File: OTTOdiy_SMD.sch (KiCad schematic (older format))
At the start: 20 parts, among them J201 RASPBERRY PI 3 A+

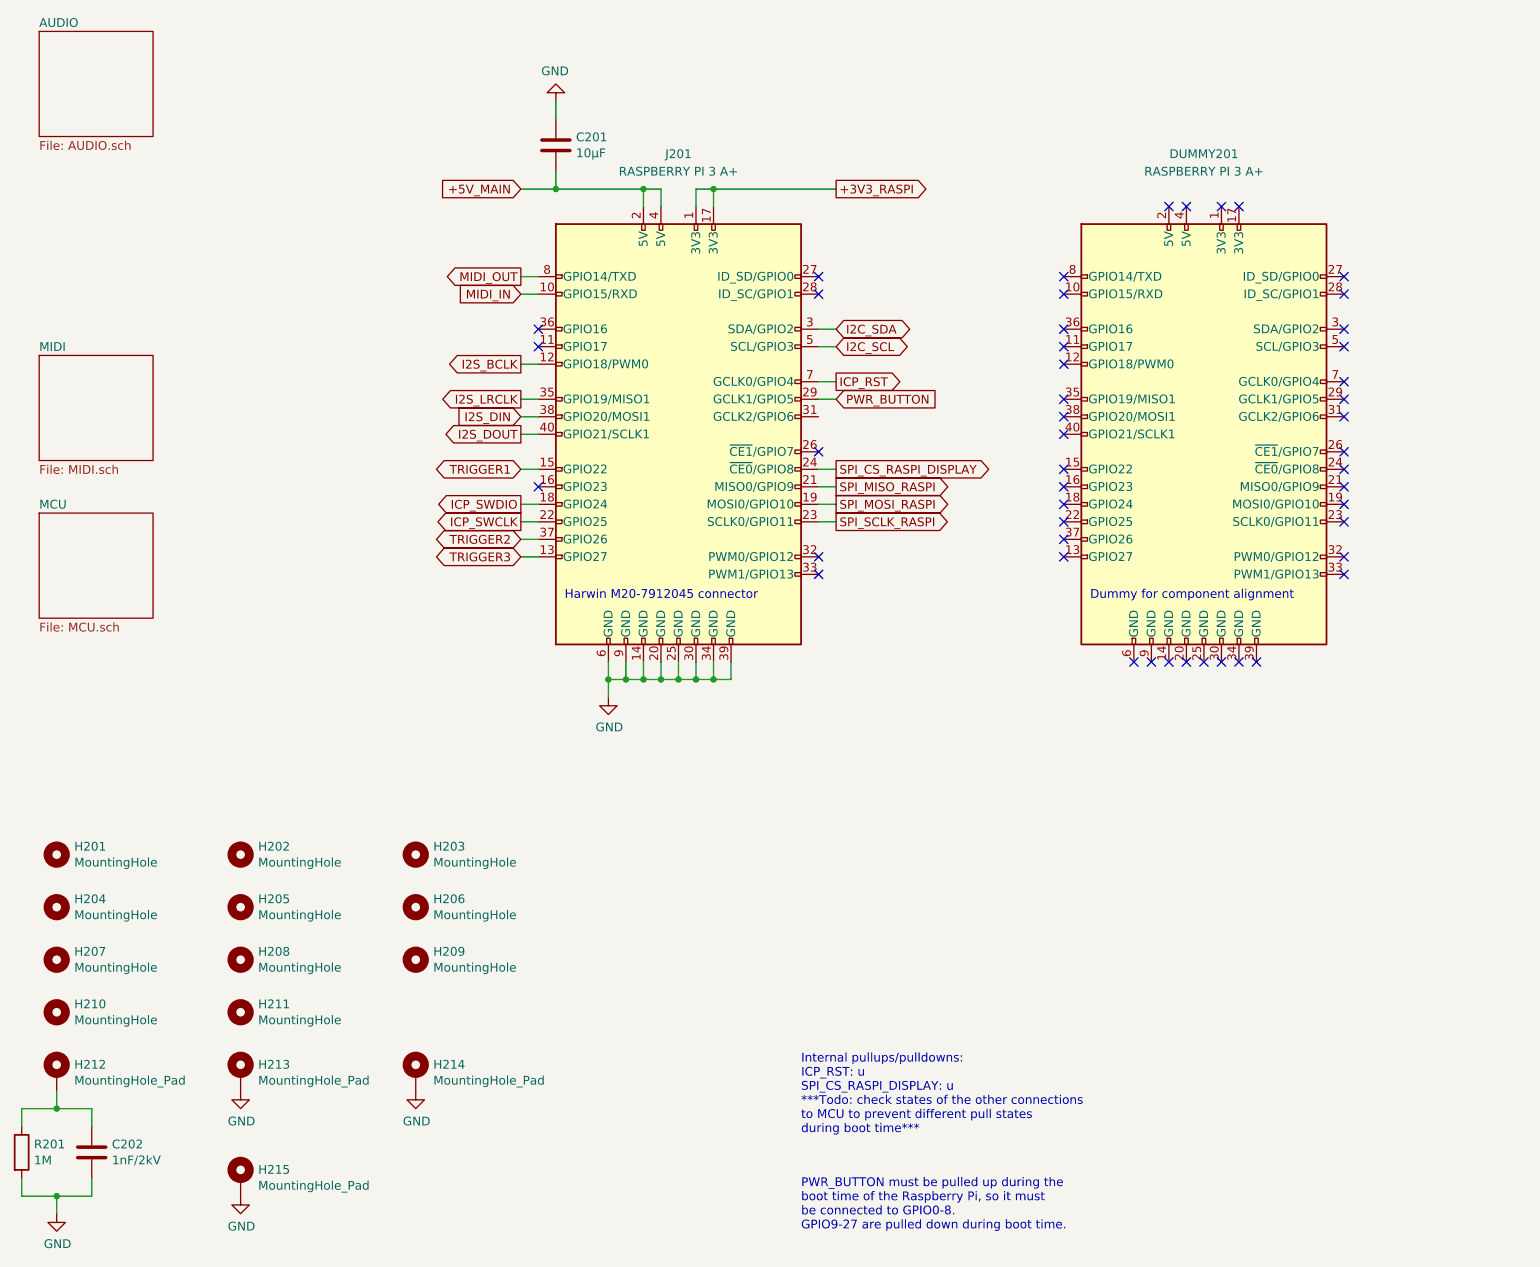
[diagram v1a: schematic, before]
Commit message: PWR entry, ESD, JTAG, PU/PDs modified. Review pass 1
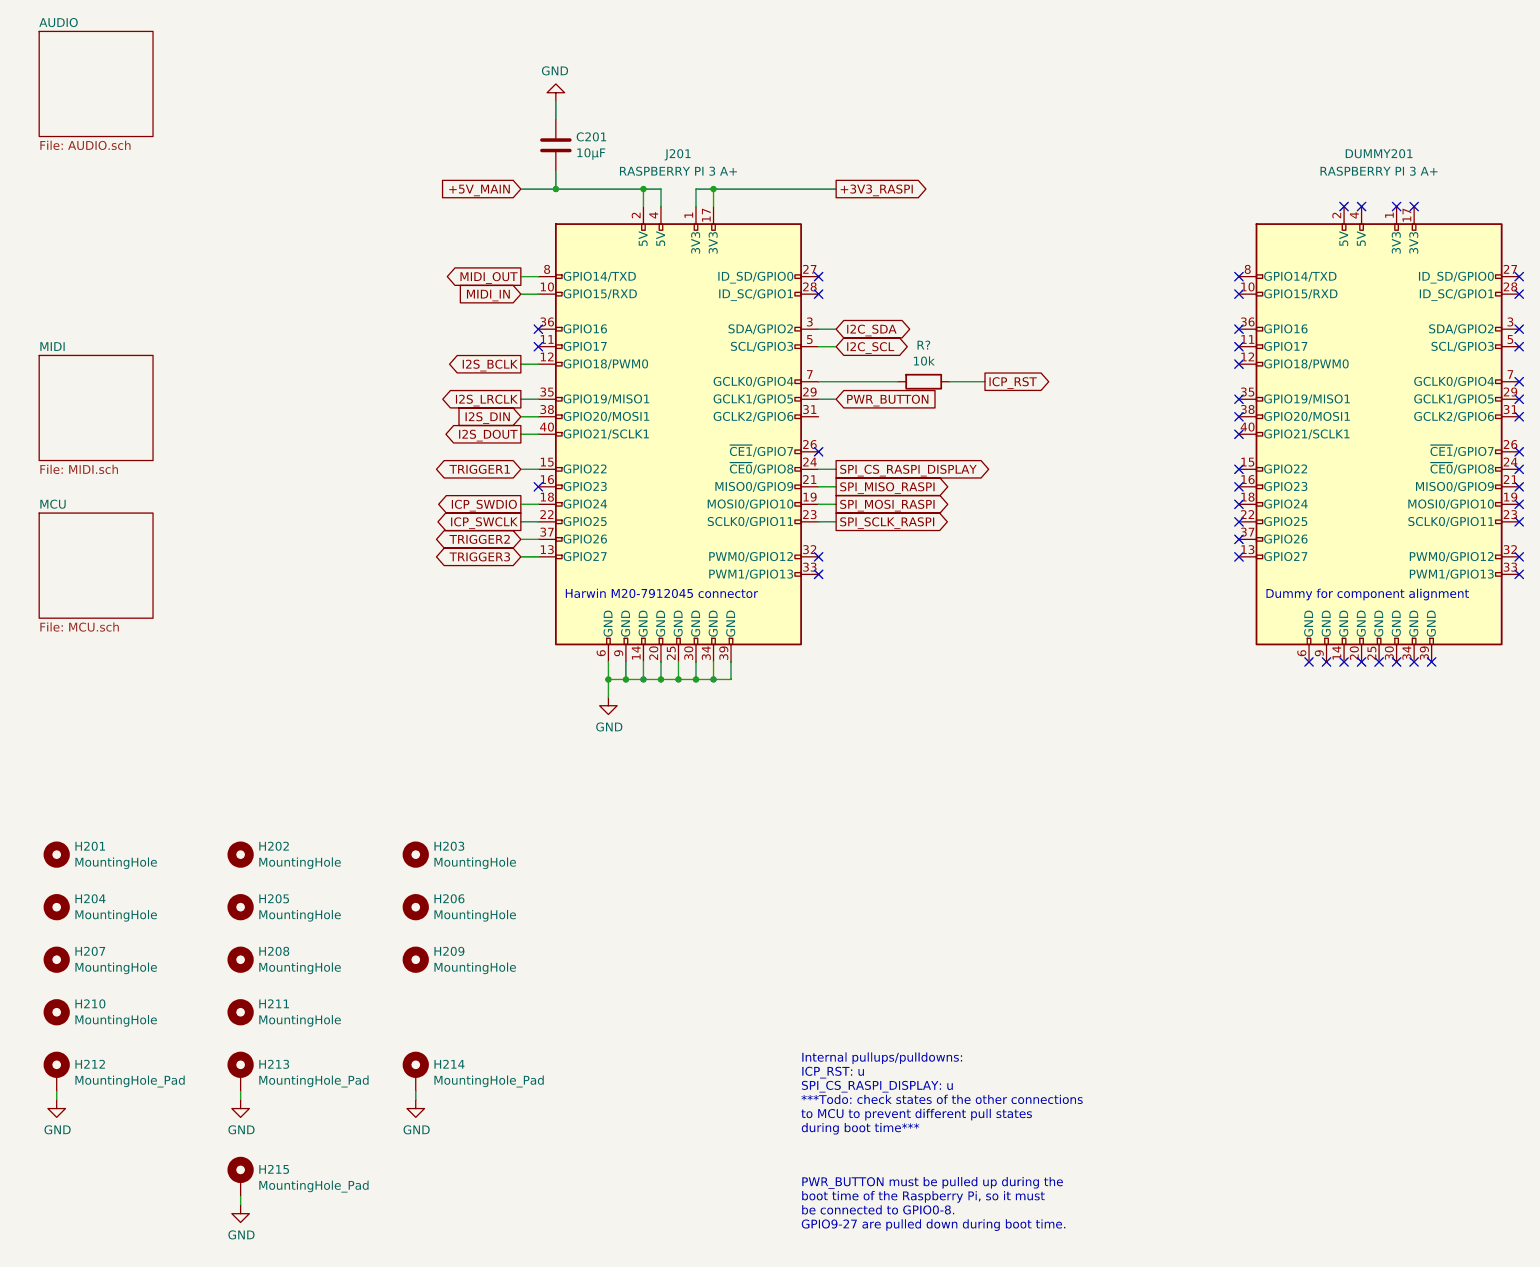
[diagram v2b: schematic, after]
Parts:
- removed C202: 1nF/2kV, Capacitor_SMD:C_1206_3216Metric_Pad1.42x1.75mm_HandSolder, symbol Device:C
- removed R201: 1M, Resistor_SMD:R_1206_3216Metric_Pad1.42x1.75mm_HandSolder, symbol Device:R
- added R?: 10k, symbol Device:R
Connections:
- net GND: now also H212.1
- net ICP_RST: now also R?.1; no longer J201.7 (GCLK0/GPIO4)
- new net: J201.7 (GCLK0/GPIO4), R?.2
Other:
- moved on the sheet: DUMMY201
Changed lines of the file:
@@
 $EndComp
-Wire Wire Line
-	5250 2750 5150 2750
 Wire Wire Line
 	5150 2850 5250 2850
@@
 $EndSheet
 $Comp
-L Device:R R201
-U 1 1 5C6B90EE
-P 600 7150
-F 0 "R201" H 670 7196 50  0000 L CNN
-F 1 "1M" H 670 7105 50  0000 L CNN
-F 2 "Resistor_SMD:R_1206_3216Metric_Pad1.42x1.75mm_HandSolder" V 530 7150 50  0001 C CNN
-F 3 "~" H 600 7150 50  0001 C CNN
-	1    600  7150
-	1    0    0    -1
-$EndComp
-$Comp
-L Device:C C202
-U 1 1 5C6B9145
-P 1000 7150
-F 0 "C202" H 1115 7196 50  0000 L CNN
-F 1 "1nF/2kV" H 1115 7105 50  0000 L CNN
-F 2 "Capacitor_SMD:C_1206_3216Metric_Pad1.42x1.75mm_HandSolder" H 1038 7000 50  0001 C CNN
-F 3 "~" H 1000 7150 50  0001 C CNN
-	1    1000 7150
-	1    0    0    -1
-$EndComp
-Wire Wire Line
-	600  7000 600  6900
-Wire Wire Line
-	600  6900 800  6900
-Wire Wire Line
-	800  6900 800  6800
-Wire Wire Line
-	1000 7000 1000 6900
-Wire Wire Line
-	1000 6900 800  6900
-Connection ~ 800  6900
-Wire Wire Line
-	600  7300 600  7400
-Wire Wire Line
-	1000 7400 1000 7300
-Wire Wire Line
-	600  7400 800  7400
-$Comp
 L power:GND #PWR0206
 U 1 1 5C6C4424
-P 800 7500
-F 0 "#PWR0206" H 800 7250 50  0001 C CNN
-F 1 "GND" H 805 7327 50  0000 C CNN
-F 2 "" H 800 7500 50  0001 C CNN
-F 3 "" H 800 7500 50  0001 C CNN
-	1    800  7500
-	1    0    0    -1
-$EndComp
-Wire Wire Line
-	800  7500 800  7400
-Connection ~ 800  7400
-Wire Wire Line
-	800  7400 1000 7400
+P 800 6850
+F 0 "#PWR0206" H 800 6600 50  0001 C CNN
+F 1 "GND" H 805 6677 50  0000 C CNN
+F 2 "" H 800 6850 50  0001 C CNN
+F 3 "" H 800 6850 50  0001 C CNN
+	1    800  6850
+	1    0    0    -1
+$EndComp
 $Comp
 L Mechanical:MountingHole H201
@@
 Wire Wire Line
 	4550 4450 4650 4450
-Text GLabel 5250 2750 2    50   Output ~ 0
+Text GLabel 6100 2750 2    50   Output ~ 0
 ICP_RST
 Text GLabel 3450 3450 0    50   Output ~ 0
@@
 L power:GND #PWR0203
 U 1 1 5DFC7588
-P 1850 6800
-F 0 "#PWR0203" H 1850 6550 50  0001 C CNN
-F 1 "GND" H 1855 6627 50  0000 C CNN
-F 2 "" H 1850 6800 50  0001 C CNN
-F 3 "" H 1850 6800 50  0001 C CNN
-	1    1850 6800
+P 1850 6850
+F 0 "#PWR0203" H 1850 6600 50  0001 C CNN
+F 1 "GND" H 1855 6677 50  0000 C CNN
+F 2 "" H 1850 6850 50  0001 C CNN
+F 3 "" H 1850 6850 50  0001 C CNN
+	1    1850 6850
 	1    0    0    -1
 $EndComp
@@
 L power:GND #PWR0205
 U 1 1 5DFC8611
-P 1850 7400
-F 0 "#PWR0205" H 1850 7150 50  0001 C CNN
-F 1 "GND" H 1855 7227 50  0000 C CNN
-F 2 "" H 1850 7400 50  0001 C CNN
-F 3 "" H 1850 7400 50  0001 C CNN
-	1    1850 7400
+P 1850 7450
+F 0 "#PWR0205" H 1850 7200 50  0001 C CNN
+F 1 "GND" H 1855 7277 50  0000 C CNN
+F 2 "" H 1850 7450 50  0001 C CNN
+F 3 "" H 1850 7450 50  0001 C CNN
+	1    1850 7450
 	1    0    0    -1
 $EndComp
@@
 L power:GND #PWR0204
 U 1 1 5E86839B
-P 2850 6800
-F 0 "#PWR0204" H 2850 6550 50  0001 C CNN
-F 1 "GND" H 2855 6627 50  0000 C CNN
-F 2 "" H 2850 6800 50  0001 C CNN
-F 3 "" H 2850 6800 50  0001 C CNN
-	1    2850 6800
+P 2850 6850
+F 0 "#PWR0204" H 2850 6600 50  0001 C CNN
+F 1 "GND" H 2855 6677 50  0000 C CNN
+F 2 "" H 2850 6850 50  0001 C CNN
+F 3 "" H 2850 6850 50  0001 C CNN
+	1    2850 6850
 	1    0    0    -1
 $EndComp
@@
 L Connector:Raspberry_Pi_2_3 DUMMY201
 U 1 1 5E18E15A
-P 7350 3050
-F 0 "DUMMY201" H 7350 4650 50  0000 C CNN
-F 1 "RASPBERRY PI 3 A+" H 7350 4550 50  0000 C CNN
-F 2 "Spatz:Raspberry Pi A" H 7350 3050 50  0001 C CNN
-F 3 "https://www.raspberrypi.org/documentation/hardware/raspberrypi/schematics/rpi_SCH_3bplus_1p0_reduced.pdf" H 7350 3050 50  0001 C CNN
-	1    7350 3050
+P 8350 3050
+F 0 "DUMMY201" H 8350 4650 50  0000 C CNN
+F 1 "RASPBERRY PI 3 A+" H 8350 4550 50  0000 C CNN
+F 2 "Spatz:Raspberry Pi A" H 8350 3050 50  0001 C CNN
+F 3 "https://www.raspberrypi.org/documentation/hardware/raspberrypi/schematics/rpi_SCH_3bplus_1p0_reduced.pdf" H 8350 3050 50  0001 C CNN
+	1    8350 3050
 	1    0    0    -1
 $EndComp
@@
 Wire Wire Line
 	3450 1650 3650 1650
-NoConn ~ 7150 1750
-NoConn ~ 7250 1750
-NoConn ~ 7450 1750
-NoConn ~ 7550 1750
-NoConn ~ 6550 2150
-NoConn ~ 6550 2250
-NoConn ~ 6550 2450
-NoConn ~ 6550 2550
-NoConn ~ 6550 2650
-NoConn ~ 6550 2850
-NoConn ~ 6550 2950
-NoConn ~ 6550 3050
-NoConn ~ 6550 3250
-NoConn ~ 6550 3350
-NoConn ~ 6550 3450
-NoConn ~ 6550 3550
-NoConn ~ 6550 3650
-NoConn ~ 6550 3750
-NoConn ~ 8150 3850
-NoConn ~ 8150 3750
-NoConn ~ 8150 3550
-NoConn ~ 8150 3450
-NoConn ~ 8150 3350
-NoConn ~ 8150 3250
-NoConn ~ 8150 3150
-NoConn ~ 8150 2950
-NoConn ~ 8150 2850
-NoConn ~ 8150 2750
-NoConn ~ 8150 2550
-NoConn ~ 8150 2450
-NoConn ~ 8150 2250
-NoConn ~ 8150 2150
-NoConn ~ 6950 4350
-NoConn ~ 7050 4350
-NoConn ~ 7150 4350
-NoConn ~ 7250 4350
-NoConn ~ 7350 4350
-NoConn ~ 7450 4350
-NoConn ~ 7550 4350
-NoConn ~ 7650 4350
-Text Notes 6700 4000 0    50   ~ 0
+NoConn ~ 8150 1750
+NoConn ~ 8250 1750
+NoConn ~ 8450 1750
+NoConn ~ 8550 1750
+NoConn ~ 7550 2150
+NoConn ~ 7550 2250
+NoConn ~ 7550 2450
+NoConn ~ 7550 2550
+NoConn ~ 7550 2650
+NoConn ~ 7550 2850
+NoConn ~ 7550 2950
+NoConn ~ 7550 3050
+NoConn ~ 7550 3250
+NoConn ~ 7550 3350
+NoConn ~ 7550 3450
+NoConn ~ 7550 3550
+NoConn ~ 7550 3650
+NoConn ~ 7550 3750
+NoConn ~ 9150 3850
+NoConn ~ 9150 3750
+NoConn ~ 9150 3550
+NoConn ~ 9150 3450
+NoConn ~ 9150 3350
+NoConn ~ 9150 3250
+NoConn ~ 9150 3150
+NoConn ~ 9150 2950
+NoConn ~ 9150 2850
+NoConn ~ 9150 2750
+NoConn ~ 9150 2550
+NoConn ~ 9150 2450
+NoConn ~ 9150 2250
+NoConn ~ 9150 2150
+NoConn ~ 7950 4350
+NoConn ~ 8050 4350
+NoConn ~ 8150 4350
+NoConn ~ 8250 4350
+NoConn ~ 8350 4350
+NoConn ~ 8450 4350
+NoConn ~ 8550 4350
+NoConn ~ 8650 4350
+Text Notes 7700 4000 0    50   ~ 0
 Dummy for component alignment
 NoConn ~ 3550 2450
@@
 NoConn ~ 5150 3750
 NoConn ~ 5150 3850
+Wire Wire Line
+	800  6800 800  6850
+Wire Wire Line
+	1850 6800 1850 6850
+Wire Wire Line
+	2850 6800 2850 6850
+Wire Wire Line
+	1850 7400 1850 7450
+$Comp
+L Device:R R?
+U 1 1 5E14AAB9
+P 5750 2750
+F 0 "R?" V 5543 2750 50  0000 C CNN
+F 1 "10k" V 5634 2750 50  0000 C CNN
+F 2 "" V 5680 2750 50  0001 C CNN
+F 3 "~" H 5750 2750 50  0001 C CNN
+	1    5750 2750
+	0    1    1    0
+$EndComp
+Wire Wire Line
+	5150 2750 5600 2750
+Wire Wire Line
+	5900 2750 6100 2750
 $EndSCHEMATC
